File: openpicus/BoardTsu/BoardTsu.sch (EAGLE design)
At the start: 16 parts, among them IC1 74HC4051DIL16, IC2 74HC4051DIL16

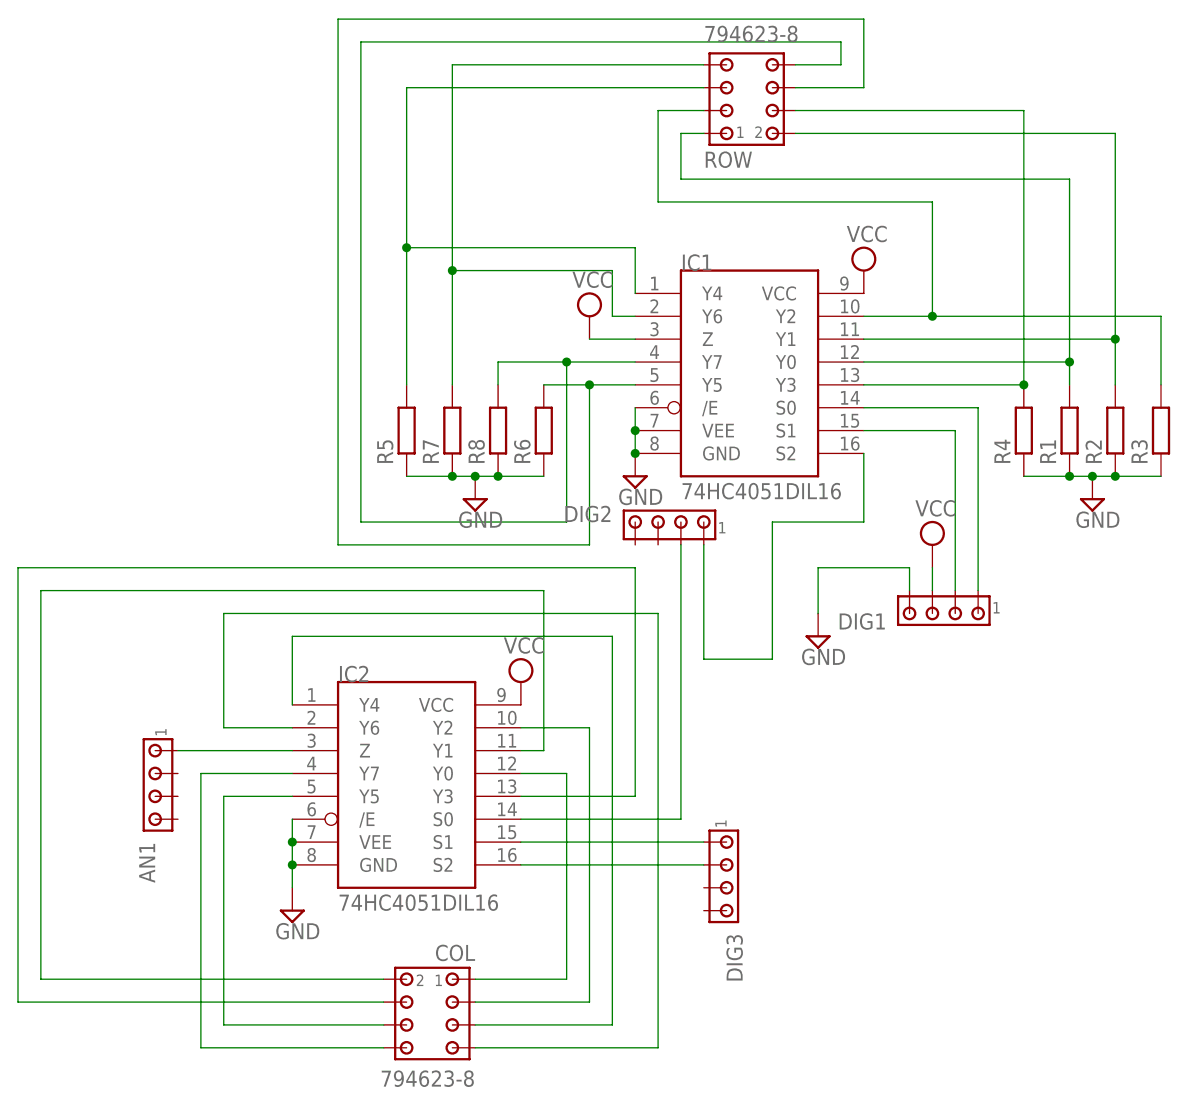
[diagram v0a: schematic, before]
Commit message: Schematic 1.0.1: fixes to power supply lines
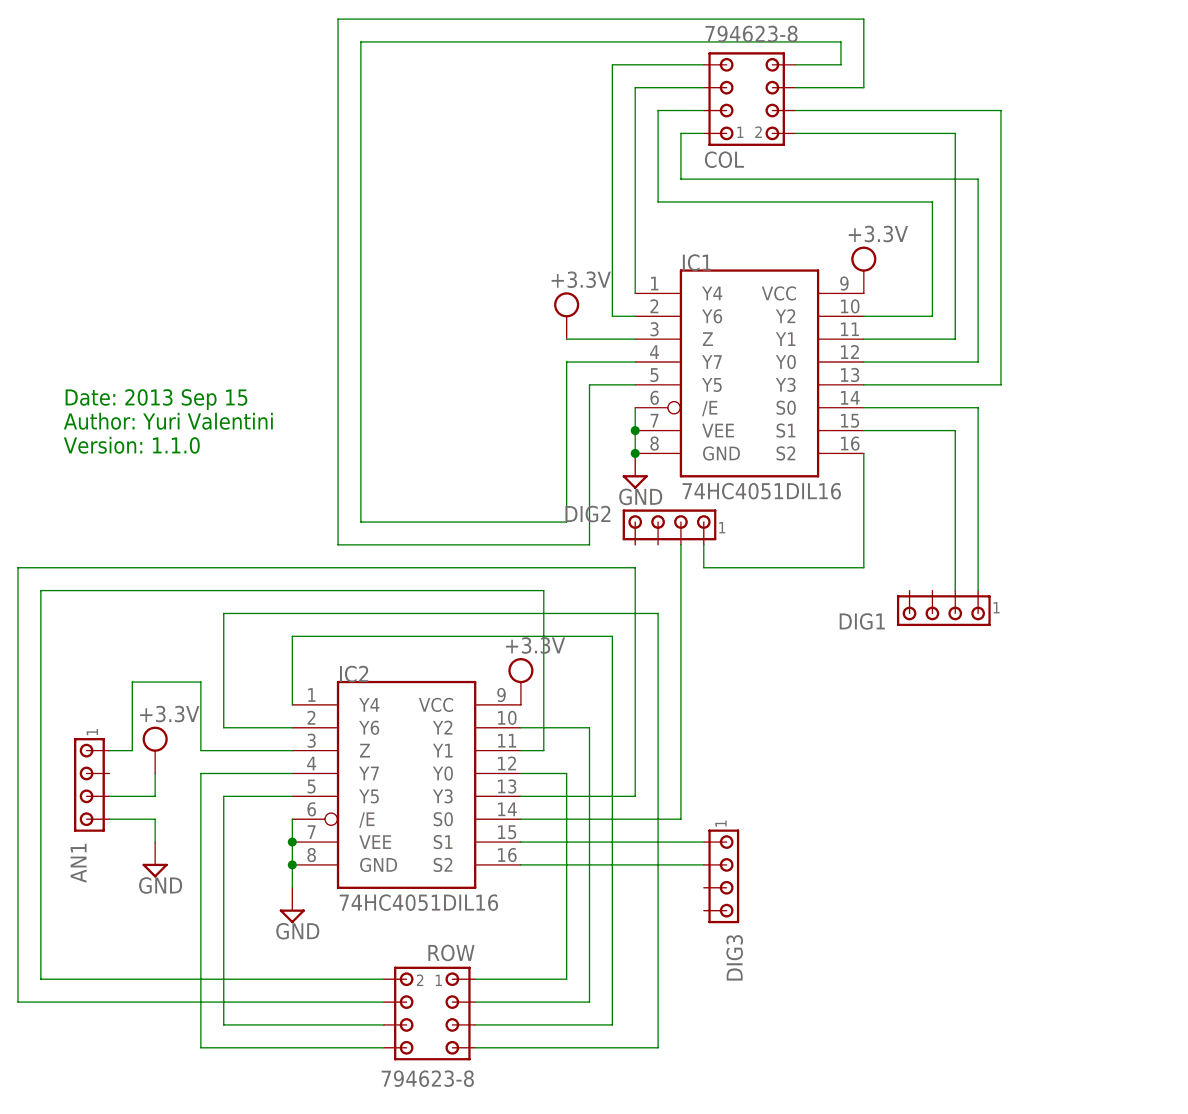
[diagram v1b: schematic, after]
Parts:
- removed R1, R2, R3, R4, R5, R6, R7, R8: (no value), resistor:R-EU_0207/10
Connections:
- net GND: now also AN1.4; no longer DIG1.4, R1.1, R2.1, R3.1, R4.1, R5.1, R6.1, R7.1, R8.1
- net N$1: now also COL.4; no longer R4.2, ROW.4
- net N$16: now also ROW.1; no longer COL.1
- net N$17: now also ROW.2; no longer COL.2
- net N$18: now also ROW.3; no longer COL.3
- net N$19: now also ROW.4; no longer COL.4
- net N$2: now also COL.1; no longer R1.2, ROW.1
- net N$20: now also ROW.5; no longer COL.5
- net N$21: now also ROW.6; no longer COL.6
- net N$23: now also ROW.7; no longer COL.7
- net N$24: now also ROW.8; no longer COL.8
- net N$3: now also COL.2; no longer R2.2, ROW.2
- net N$4: now also COL.3; no longer R3.2, ROW.3
- net N$5: now also COL.5; no longer R5.2, ROW.5
- net N$6: now also COL.6; no longer R6.2, ROW.6
- net N$7: now also COL.8; no longer R8.2, ROW.8
- net N$8: now also COL.7; no longer R7.2, ROW.7
- net VCC: now also AN1.3; no longer DIG1.3
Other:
- note added: "Date: 2013 Sep 15 Author: Yuri Valentini Version: 1.1.0"
- moved on the sheet: AN1, COL, ROW

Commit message: Renamed 74hc4051 pins on schematic
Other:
- note added: "Date: 2013 Sep 15 Author: Yuri Valentini Version: 1.2.0"
- note removed: "Date: 2013 Sep 15 Author: Yuri Valentini Version: 1.1.0"
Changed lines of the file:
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@@
 <?xml version="1.0" encoding="utf-8"?>
 <!DOCTYPE eagle SYSTEM "eagle.dtd">
-<eagle version="6.4">
+<eagle version="6.3">
 <drawing>
 <settings>
@@
 <text x="-43.18" y="66.04" size="1.778" layer="91">Date: 2013 Sep 15
 Author: Yuri Valentini
-Version: 1.1.0</text>
+Version: 1.2.0</text>
 </plain>
 <instances>

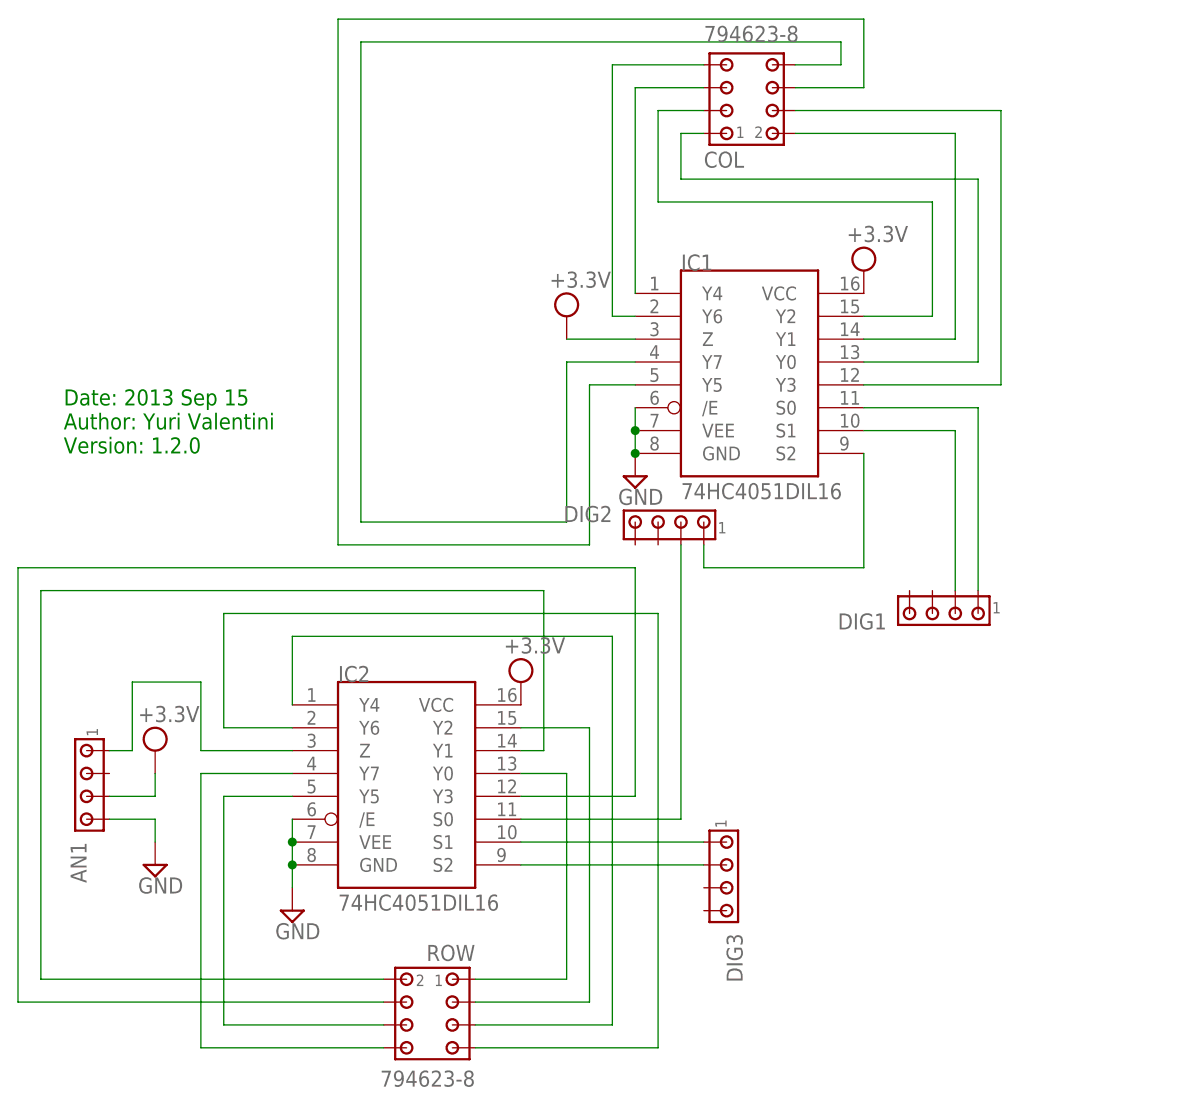
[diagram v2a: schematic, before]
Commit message: Simplified schematic routing
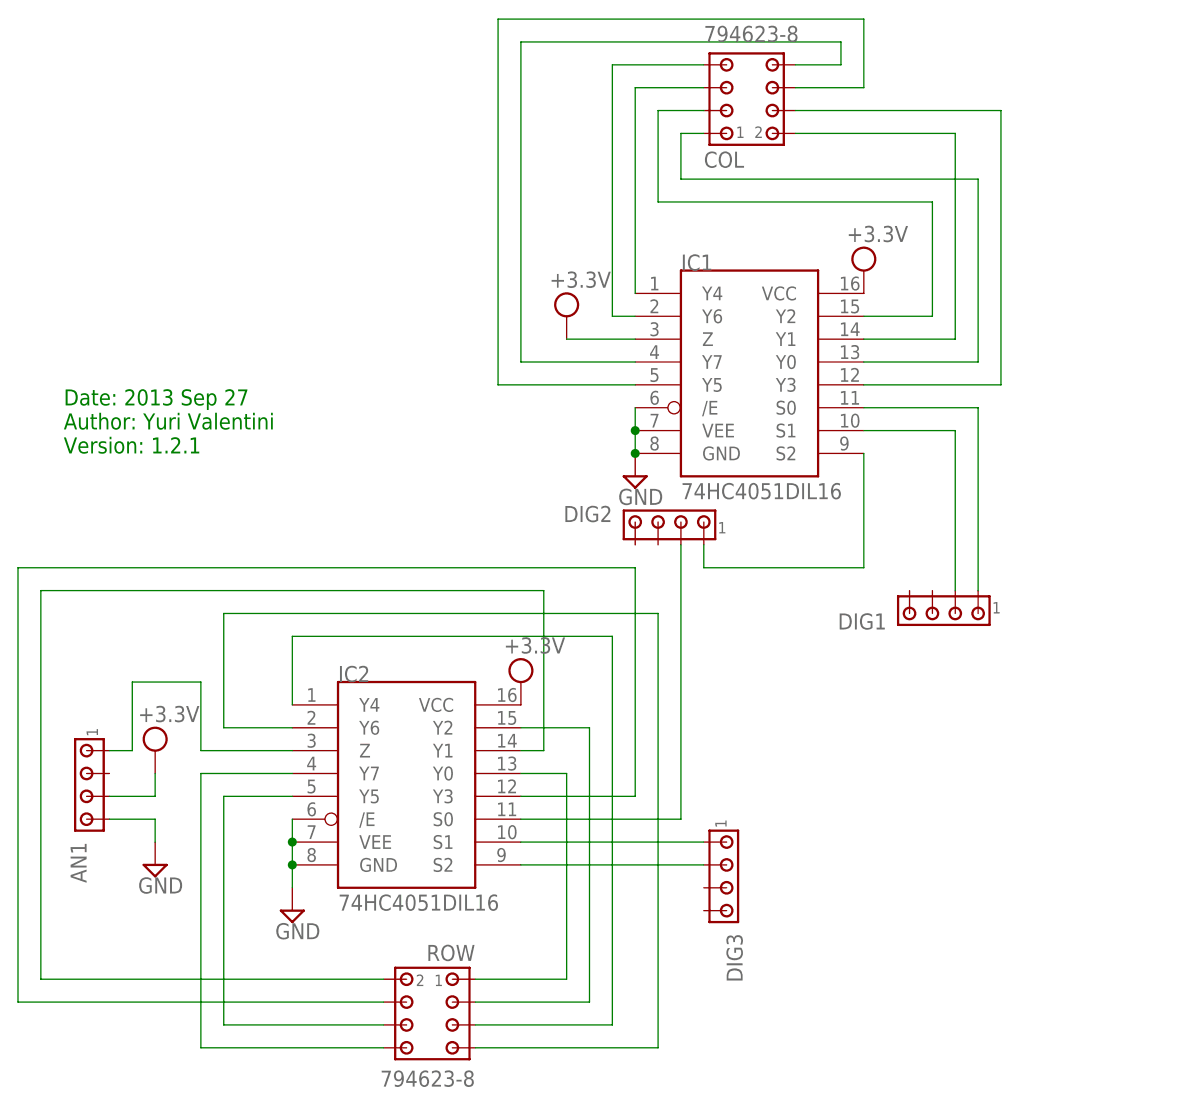
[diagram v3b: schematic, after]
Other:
- note added: "Date: 2013 Sep 27 Author: Yuri Valentini Version: 1.2.1"
- note removed: "Date: 2013 Sep 15 Author: Yuri Valentini Version: 1.2.0"
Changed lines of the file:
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@@
 <sheet>
 <plain>
-<text x="-43.18" y="66.04" size="1.778" layer="91">Date: 2013 Sep 15
+<text x="-43.18" y="66.04" size="1.778" layer="91">Date: 2013 Sep 27
 Author: Yuri Valentini
-Version: 1.2.0</text>
+Version: 1.2.1</text>
 </plain>
 <instances>
@@
 <segment>
 <pinref part="IC1" gate="G$1" pin="Y5"/>
-<wire x1="15.24" y1="73.66" x2="20.32" y2="73.66" width="0.1524" layer="91"/>
-<wire x1="15.24" y1="73.66" x2="15.24" y2="55.88" width="0.1524" layer="91"/>
-<wire x1="15.24" y1="55.88" x2="-12.7" y2="55.88" width="0.1524" layer="91"/>
-<wire x1="-12.7" y1="55.88" x2="-12.7" y2="114.3" width="0.1524" layer="91"/>
-<wire x1="-12.7" y1="114.3" x2="45.72" y2="114.3" width="0.1524" layer="91"/>
+<wire x1="20.32" y1="73.66" x2="5.08" y2="73.66" width="0.1524" layer="91"/>
+<wire x1="5.08" y1="73.66" x2="5.08" y2="114.3" width="0.1524" layer="91"/>
+<wire x1="5.08" y1="114.3" x2="45.72" y2="114.3" width="0.1524" layer="91"/>
 <wire x1="45.72" y1="114.3" x2="45.72" y2="106.68" width="0.1524" layer="91"/>
 <pinref part="COL" gate="G$1" pin="6"/>
@@
 <wire x1="38.1" y1="109.22" x2="43.18" y2="109.22" width="0.1524" layer="91"/>
 <wire x1="43.18" y1="109.22" x2="43.18" y2="111.76" width="0.1524" layer="91"/>
-<wire x1="43.18" y1="111.76" x2="-10.16" y2="111.76" width="0.1524" layer="91"/>
-<wire x1="-10.16" y1="111.76" x2="-10.16" y2="58.42" width="0.1524" layer="91"/>
-<wire x1="-10.16" y1="58.42" x2="12.7" y2="58.42" width="0.1524" layer="91"/>
+<wire x1="43.18" y1="111.76" x2="7.62" y2="111.76" width="0.1524" layer="91"/>
+<wire x1="7.62" y1="111.76" x2="7.62" y2="76.2" width="0.1524" layer="91"/>
+<wire x1="7.62" y1="76.2" x2="20.32" y2="76.2" width="0.1524" layer="91"/>
 <pinref part="IC1" gate="G$1" pin="Y7"/>
-<wire x1="12.7" y1="76.2" x2="20.32" y2="76.2" width="0.1524" layer="91"/>
-<wire x1="12.7" y1="58.42" x2="12.7" y2="76.2" width="0.1524" layer="91"/>
-</segment>
-</net>
+</segment>
+</net>
